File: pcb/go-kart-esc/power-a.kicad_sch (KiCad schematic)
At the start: 4 parts, among them Q1 IRLB8721PBF, Q2 IRLB8721PBF, Q3 IRLB8721PBF, Q4 IRLB8721PBF

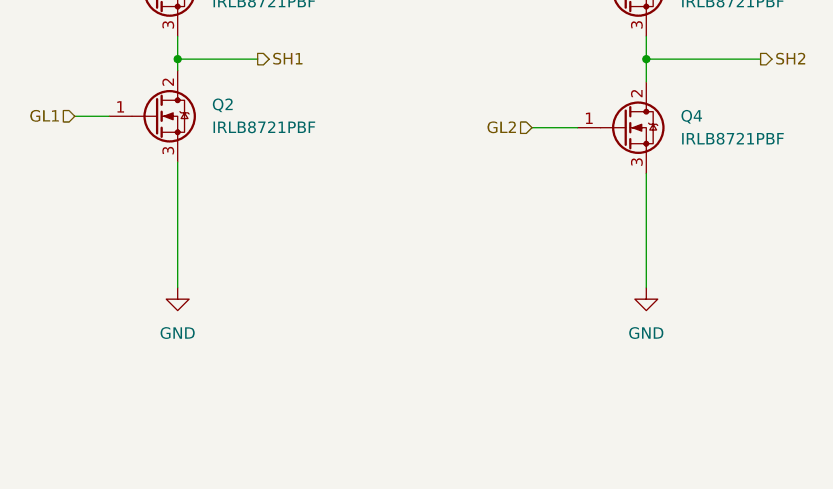
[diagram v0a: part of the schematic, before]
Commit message: Added resistor shunts
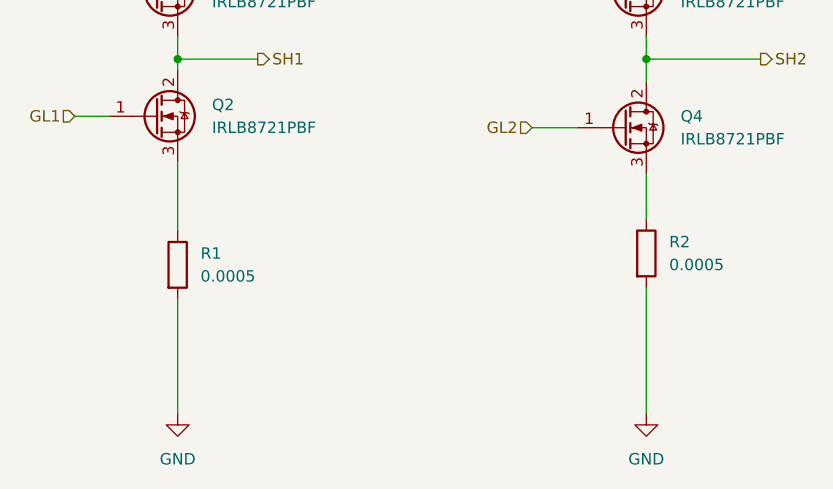
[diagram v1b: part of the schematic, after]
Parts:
- added R1, R2: 0.0005, symbol Device:R
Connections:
- net GND: now also R1.2, R2.2; no longer Q2.3 (S), Q4.3 (S)
- new net: Q4.3 (S), R2.1
- new net: Q2.3 (S), R1.1
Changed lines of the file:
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@@
     (stroke (width 0) (type default))
   )
-  (wire (pts (xy 113.03 93.98) (xy 113.03 107.95))
+  (wire (pts (xy 165.1 95.25) (xy 165.1 100.33))
+    (stroke (width 0) (type default))
+  )
+  (wire (pts (xy 113.03 93.98) (xy 113.03 101.6))
     (stroke (width 0) (type default))
   )
@@
     (stroke (width 0) (type default))
   )
+  (wire (pts (xy 113.03 109.22) (xy 113.03 121.92))
+    (stroke (width 0) (type default))
+  )
   (wire (pts (xy 113.03 82.55) (xy 121.92 82.55))
     (stroke (width 0) (type default))
@@
     (stroke (width 0) (type default))
   )
-  (wire (pts (xy 165.1 95.25) (xy 165.1 107.95))
-    (stroke (width 0) (type default))
-  )
   (wire (pts (xy 165.1 80.01) (xy 165.1 82.55))
+    (stroke (width 0) (type default))
+  )
+  (wire (pts (xy 165.1 107.95) (xy 165.1 121.92))
     (stroke (width 0) (type default))
   )
@@
     )
   )
-  (symbol (lib_id "power:GND") (at 165.1 107.95 0) (unit 1)
-    (in_bom yes) (on_board yes) (dnp no) (fields_autoplaced)
-    (property "Reference" "#PWR01" (at 165.1 114.3 0)
-      (effects (font (size 1.27 1.27)) hide)
-    )
-    (property "Value" "GND" (at 165.1 113.03 0)
+  (symbol (lib_id "power:GND") (at 165.1 121.92 0) (unit 1)
+    (in_bom yes) (on_board yes) (dnp no) (fields_autoplaced)
+    (property "Reference" "#PWR01" (at 165.1 128.27 0)
+      (effects (font (size 1.27 1.27)) hide)
+    )
+    (property "Value" "GND" (at 165.1 127 0)
       (effects (font (size 1.27 1.27)))
     )
-    (property "Footprint" "" (at 165.1 107.95 0)
-      (effects (font (size 1.27 1.27)) hide)
-    )
-    (property "Datasheet" "" (at 165.1 107.95 0)
+    (property "Footprint" "" (at 165.1 121.92 0)
+      (effects (font (size 1.27 1.27)) hide)
+    )
+    (property "Datasheet" "" (at 165.1 121.92 0)
       (effects (font (size 1.27 1.27)) hide)
     )
@@
     )
   )
-  (symbol (lib_id "power:GND") (at 113.03 107.95 0) (unit 1)
-    (in_bom yes) (on_board yes) (dnp no) (fields_autoplaced)
-    (property "Reference" "#PWR01" (at 113.03 114.3 0)
-      (effects (font (size 1.27 1.27)) hide)
-    )
-    (property "Value" "GND" (at 113.03 113.03 0)
+  (symbol (lib_id "power:GND") (at 113.03 121.92 0) (unit 1)
+    (in_bom yes) (on_board yes) (dnp no) (fields_autoplaced)
+    (property "Reference" "#PWR01" (at 113.03 128.27 0)
+      (effects (font (size 1.27 1.27)) hide)
+    )
+    (property "Value" "GND" (at 113.03 127 0)
       (effects (font (size 1.27 1.27)))
     )
-    (property "Footprint" "" (at 113.03 107.95 0)
-      (effects (font (size 1.27 1.27)) hide)
-    )
-    (property "Datasheet" "" (at 113.03 107.95 0)
+    (property "Footprint" "" (at 113.03 121.92 0)
+      (effects (font (size 1.27 1.27)) hide)
+    )
+    (property "Datasheet" "" (at 113.03 121.92 0)
       (effects (font (size 1.27 1.27)) hide)
     )
@@
     )
   )
+  (symbol (lib_id "Device:R") (at 165.1 104.14 0) (unit 1)
+    (in_bom yes) (on_board yes) (dnp no) (fields_autoplaced)
+    (property "Reference" "R2" (at 167.64 102.87 0)
+      (effects (font (size 1.27 1.27)) (justify left))
+    )
+    (property "Value" "0.0005" (at 167.64 105.41 0)
+      (effects (font (size 1.27 1.27)) (justify left))
+    )
+    (property "Footprint" "" (at 163.322 104.14 90)
+      (effects (font (size 1.27 1.27)) hide)
+    )
+    (property "Datasheet" "~" (at 165.1 104.14 0)
+      (effects (font (size 1.27 1.27)) hide)
+    )
+    (pin "1")
+    (pin "2")
+    (instances
+      (project "go-kart-esc"
+        (path "/5a70b585-4866-4f79-8013-f2242aeded57/2f2eb473-a6d5-4b09-8c58-ce0c11f580af"
+          (reference "R2") (unit 1)
+        )
+      )
+    )
+  )
   (symbol (lib_id "Transistor_FET:IRLB8721PBF") (at 162.56 74.93 0) (unit 1)
     (in_bom yes) (on_board yes) (dnp no) (fields_autoplaced)
@@
         )
       )
+    )
+  )
+  (symbol (lib_id "Device:R") (at 113.03 105.41 0) (unit 1)
+    (in_bom yes) (on_board yes) (dnp no) (fields_autoplaced)
+    (property "Reference" "R1" (at 115.57 104.14 0)
+      (effects (font (size 1.27 1.27)) (justify left))
+    )
+    (property "Value" "0.0005" (at 115.57 106.68 0)
+      (effects (font (size 1.27 1.27)) (justify left))
+    )
+    (property "Footprint" "" (at 111.252 105.41 90)
+      (effects (font (size 1.27 1.27)) hide)
+    )
+    (property "Datasheet" "~" (at 113.03 105.41 0)
+      (effects (font (size 1.27 1.27)) hide)
+    )
+    (pin "1")
+    (pin "2")
+    (instances
+      (project "go-kart-esc"
+        (path "/5a70b585-4866-4f79-8013-f2242aeded57/2f2eb473-a6d5-4b09-8c58-ce0c11f580af"
+          (reference "R1") (unit 1)
+        )
+      )

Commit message: Poggers
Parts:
- removed R1: 0.0005, symbol Device:R
- added C10, C9: 220u, symbol Device:C_Polarized
- added C3: 0.1u, symbol Device:C
- added C4: 4.7n, symbol Device:C
- added J1, J2: ~, symbol ESC:MotorTab
- added R1: 0.0005, symbol Device:R_Shunt
- added R3, R5: 10k, symbol Device:R
- added R4: 100, symbol Device:R
- added TH1: 10k, symbol Device:Thermistor_NTC
- added U2: ~, symbol ESC:INA185
- R2: value 0.0005 -> 10k
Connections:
- net GND: now also C10.2, C3.2, C4.2, C9.2, R1.4, R3.2, R5.2, U2.2 (GND); no longer R2.2
- net SH1: now also J1.1
- net SH2: now also J2.1
- net +3V3: now reaches R2.1
- net +3V3: now also C3.1, TH1.1, U2.6 (V+); no longer Q4.3 (S)
- net MOTOR_LOW: now reaches Q2.3 (S)
- net MOTOR_LOW: now also Q4.3 (S), R1.1
- net at Q1.2 (D): now also C9.1
- net at Q3.2 (D): now also C10.1
- new net C: R4.1, U2.1
- new net CURR: C4.1, R4.2
- new net SHUNT+: R1.2, U2.3 (+)
- new net SHUNT-: R1.3, U2.4 (-)
- new net TEMP: R5.1, TH1.2
- new net VREF: R2.2, R3.1, U2.5 (REF)
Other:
- moved on the sheet: Q1, Q2

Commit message: ooga booga
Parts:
- removed J1, J2: ~, symbol ESC:MotorTab
- removed Q1, Q2, Q3, Q4: IRLB8721PBF, Package_TO_SOT_THT:TO-220-3_Vertical, symbol Transistor_FET:IRLB8721PBF
- added J301: MOTOR_A+, ESC:Motor_Solder_Pad, symbol Connector_Generic:Conn_01x01
- added J302: MOTOR_A-, ESC:Motor_Solder_Pad, symbol Connector_Generic:Conn_01x01
- added Q301, Q302, Q303, Q304: CSD19533Q5A, Package_TO_SOT_SMD:TDSON-8-1, symbol Transistor_FET:CSD19533Q5A
- C301: renamed from C3; footprint (none) -> Capacitor_SMD:C_0402_1005Metric_Pad0.74x0.62mm_HandSolder
- C302: renamed from C9; footprint (none) -> Capacitor_THT:CP_Radial_D10.0mm_P5.00mm
- C303: renamed from C4; footprint (none) -> Capacitor_SMD:C_0603_1608Metric_Pad1.08x0.95mm_HandSolder
- C304: renamed from C10; footprint (none) -> Capacitor_THT:CP_Radial_D10.0mm_P5.00mm
- R301: renamed from R1; value 0.0005 -> 0.00025; footprint (none) -> ESC:Shunt_2725
- R302: renamed from R4; footprint (none) -> Resistor_SMD:R_0402_1005Metric_Pad0.72x0.64mm_HandSolder
- R303: renamed from R2; footprint (none) -> Resistor_SMD:R_0402_1005Metric_Pad0.72x0.64mm_HandSolder
- R304: renamed from R3; footprint (none) -> Resistor_SMD:R_0402_1005Metric_Pad0.72x0.64mm_HandSolder
- R305: renamed from R5; footprint (none) -> Resistor_SMD:R_0402_1005Metric_Pad0.72x0.64mm_HandSolder
- TH301: renamed from TH1; footprint (none) -> Resistor_SMD:R_0201_0603Metric_Pad0.64x0.40mm_HandSolder
- U301: renamed from U2; value ~ -> INA185A2QDCKRQ1; footprint (none) -> Package_TO_SOT_SMD:SOT-363_SC-70-6_Handsoldering
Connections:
- net GH1: now also Q301.4 (G)
- net GH2: now also Q303.4 (G)
- net GL1: now also Q302.4 (G)
- net GL2: now also Q304.4 (G)
- net MOTOR_LOW: now also Q302.1 (S), Q302.2 (S), Q302.3 (S), Q304.1 (S), Q304.2 (S), Q304.3 (S)
- net SH1: now also J301.1 (Pin_1), Q301.1 (S), Q301.2 (S), Q301.3 (S), Q302.5 (D)
- net SH2: now also J302.1 (Pin_1), Q303.1 (S), Q303.2 (S), Q303.3 (S), Q304.5 (D)
- net +BATT: now reaches C302.1
- net +BATT: now also C304.1, Q301.5 (D), Q303.5 (D)
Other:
- note added: "Gain: x50"

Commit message: ooga booga
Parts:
- removed R301: 0.00025, ESC:Shunt_2725, symbol Device:R_Shunt
- added R301: 0.00025, ESC:Shunt_2725, symbol Device:R
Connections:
- net SHUNT+ is gone; now on net +3V3: U301.3 (V+)
- net SHUNT- is gone; now on net MOTOR_LOW: U301.4 (+)
- net +3V3: no longer U301.6 (V+)
- net C: now also U301.6; no longer U301.1
- net GND: now also U301.5 (-), R301.1
- net MOTOR_LOW: now also R301.2
- net VREF: now also U301.1 (REF); no longer U301.5 (REF)
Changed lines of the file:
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@@
   (junction (at 165.1 82.55) (diameter 0) (color 0 0 0 0)
   )
+  (junction (at 113.03 128.27) (diameter 0) (color 0 0 0 0)
+  )
   (junction (at 162.56 123.19) (diameter 0) (color 0 0 0 0)
   )
@@
   (junction (at 90.17 81.28) (diameter 0) (color 0 0 0 0)
   )
+  (junction (at 113.03 116.84) (diameter 0) (color 0 0 0 0)
+  )
   (junction (at 113.03 100.33) (diameter 0) (color 0 0 0 0)
   )
@@
     (stroke (width 0) (type default))
   )
+  (wire (pts (xy 116.84 128.27) (xy 113.03 128.27))
+    (stroke (width 0) (type default))
+  )
+  (wire (pts (xy 113.03 116.84) (xy 113.03 119.38))
+    (stroke (width 0) (type default))
+  )
+  (wire (pts (xy 116.84 116.84) (xy 113.03 116.84))
+    (stroke (width 0) (type default))
+  )
   (wire (pts (xy 138.43 130.81) (xy 138.43 133.35))
     (stroke (width 0) (type default))
   )
+  (wire (pts (xy 116.84 125.73) (xy 116.84 128.27))
+    (stroke (width 0) (type default))
+  )
   (wire (pts (xy 143.51 123.19) (xy 151.13 123.19))
     (stroke (width 0) (type default))
@@
     (stroke (width 0) (type default))
   )
+  (wire (pts (xy 116.84 120.65) (xy 116.84 116.84))
+    (stroke (width 0) (type default))
+  )
   (wire (pts (xy 152.4 90.17) (xy 157.48 90.17))
     (stroke (width 0) (type default))
   )
+  (wire (pts (xy 113.03 128.27) (xy 113.03 135.89))
+    (stroke (width 0) (type default))
+  )
   (wire (pts (xy 229.87 123.19) (xy 237.49 123.19))
     (stroke (width 0) (type default))
@@
     (stroke (width 0) (type default))
   )
-  (wire (pts (xy 113.03 128.27) (xy 113.03 135.89))
+  (wire (pts (xy 113.03 127) (xy 113.03 128.27))
     (stroke (width 0) (type default))
   )
@@
     (stroke (width 0) (type default))
   )
-  (wire (pts (xy 113.03 100.33) (xy 113.03 118.11))
+  (wire (pts (xy 113.03 100.33) (xy 113.03 116.84))
     (stroke (width 0) (type default))
   )
@@
   (symbol (lib_id "power:+BATT") (at 86.36 64.77 0) (unit 1)
     (in_bom yes) (on_board yes) (dnp no) (fields_autoplaced)
-    (property "Reference" "#PWR0609" (at 86.36 68.58 0)
+    (property "Reference" "#PWR0601" (at 86.36 68.58 0)
       (effects (font (size 1.27 1.27)) hide)
     )
@@
       (project "go-kart-esc"
         (path "/5a70b585-4866-4f79-8013-f2242aeded57/a459c41b-c6c3-40c7-8485-5a95e06155ac"
-          (reference "#PWR0609") (unit 1)
-        )
-        (path "/5a70b585-4866-4f79-8013-f2242aeded57/2f2eb473-a6d5-4b09-8c58-ce0c11f580af"
-          (reference "#PWR0309") (unit 1)
+          (reference "#PWR0601") (unit 1)
+        )
+        (path "/5a70b585-4866-4f79-8013-f2242aeded57/2f2eb473-a6d5-4b09-8c58-ce0c11f580af"
+          (reference "#PWR0301") (unit 1)
         )
       )
@@
   (symbol (lib_id "power:+BATT") (at 165.1 66.04 0) (unit 1)
     (in_bom yes) (on_board yes) (dnp no) (fields_autoplaced)
-    (property "Reference" "#PWR0601" (at 165.1 69.85 0)
+    (property "Reference" "#PWR0609" (at 165.1 69.85 0)
       (effects (font (size 1.27 1.27)) hide)
     )
@@
       (project "go-kart-esc"
         (path "/5a70b585-4866-4f79-8013-f2242aeded57/a459c41b-c6c3-40c7-8485-5a95e06155ac"
-          (reference "#PWR0601") (unit 1)
-        )
-        (path "/5a70b585-4866-4f79-8013-f2242aeded57/2f2eb473-a6d5-4b09-8c58-ce0c11f580af"
-          (reference "#PWR0301") (unit 1)
+          (reference "#PWR0609") (unit 1)
+        )
+        (path "/5a70b585-4866-4f79-8013-f2242aeded57/2f2eb473-a6d5-4b09-8c58-ce0c11f580af"
+          (reference "#PWR0309") (unit 1)
         )
       )
@@
     )
   )
-  (symbol (lib_id "Device:R_Shunt") (at 113.03 123.19 0) (unit 1)
-    (in_bom yes) (on_board yes) (dnp no) (fields_autoplaced)
-    (property "Reference" "R301" (at 110.49 121.92 0)
-      (effects (font (size 1.27 1.27)) (justify right))
-    )
-    (property "Value" "0.00025" (at 110.49 124.46 0)
-      (effects (font (size 1.27 1.27)) (justify right))
-    )
-    (property "Footprint" "ESC:Shunt_2725" (at 111.252 123.19 90)
-      (effects (font (size 1.27 1.27)) hide)
-    )
-    (property "Datasheet" "~" (at 113.03 123.19 0)
-      (effects (font (size 1.27 1.27)) hide)
-    )
-    (pin "1")
-    (pin "2")
-    (pin "3")
-    (pin "4")
-    (instances
-      (project "go-kart-esc"
-        (path "/5a70b585-4866-4f79-8013-f2242aeded57/2f2eb473-a6d5-4b09-8c58-ce0c11f580af"
-          (reference "R301") (unit 1)
-        )
-        (path "/5a70b585-4866-4f79-8013-f2242aeded57/a459c41b-c6c3-40c7-8485-5a95e06155ac"
-          (reference "R601") (unit 1)
-        )
-      )
-    )
-  )
   (symbol (lib_id "Transistor_FET:CSD19533Q5A") (at 83.82 73.66 0) (unit 1)
     (in_bom yes) (on_board yes) (dnp no) (fields_autoplaced)
@@
         )
       )
+    )
+  )
+  (symbol (lib_id "Device:R") (at 113.03 123.19 180) (unit 1)
+    (in_bom yes) (on_board yes) (dnp no)
+    (property "Reference" "R301" (at 106.68 121.92 0)
+      (effects (font (size 1.27 1.27)) (justify right))
+    )
+    (property "Value" "0.00025" (at 102.87 124.46 0)
+      (effects (font (size 1.27 1.27)) (justify right))
+    )
+    (property "Footprint" "ESC:Shunt_2725" (at 114.808 123.19 90)
+      (effects (font (size 1.27 1.27)) hide)
+    )
+    (property "Datasheet" "~" (at 113.03 123.19 0)
+      (effects (font (size 1.27 1.27)) hide)
+    )
+    (pin "1")
+    (pin "2")
+    (instances
+      (project "go-kart-esc"
+        (path "/5a70b585-4866-4f79-8013-f2242aeded57/2f2eb473-a6d5-4b09-8c58-ce0c11f580af"
+          (reference "R301") (unit 1)
+        )
+        (path "/5a70b585-4866-4f79-8013-f2242aeded57/a459c41b-c6c3-40c7-8485-5a95e06155ac"
+          (reference "R601") (unit 1)
+        )
+      )
+      (project "simulation"
+        (path "/708b3adf-a477-436e-b5ed-8e1ccf99b3d7"
+          (reference "R3") (unit 1)
+        )
+      )

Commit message: Finished PCB
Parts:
- TH301: footprint Resistor_SMD:R_0201_0603Metric_Pad0.64x0.40mm_HandSolder -> Resistor_SMD:R_0402_1005Metric_Pad0.72x0.64mm_HandSolder
